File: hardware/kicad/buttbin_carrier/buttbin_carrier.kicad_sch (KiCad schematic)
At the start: 49 parts, among them J1 USB-C 6P, U1 TP4056, U3 TPS7A0333DBVR, U4 TB-03F-AT_Mesh

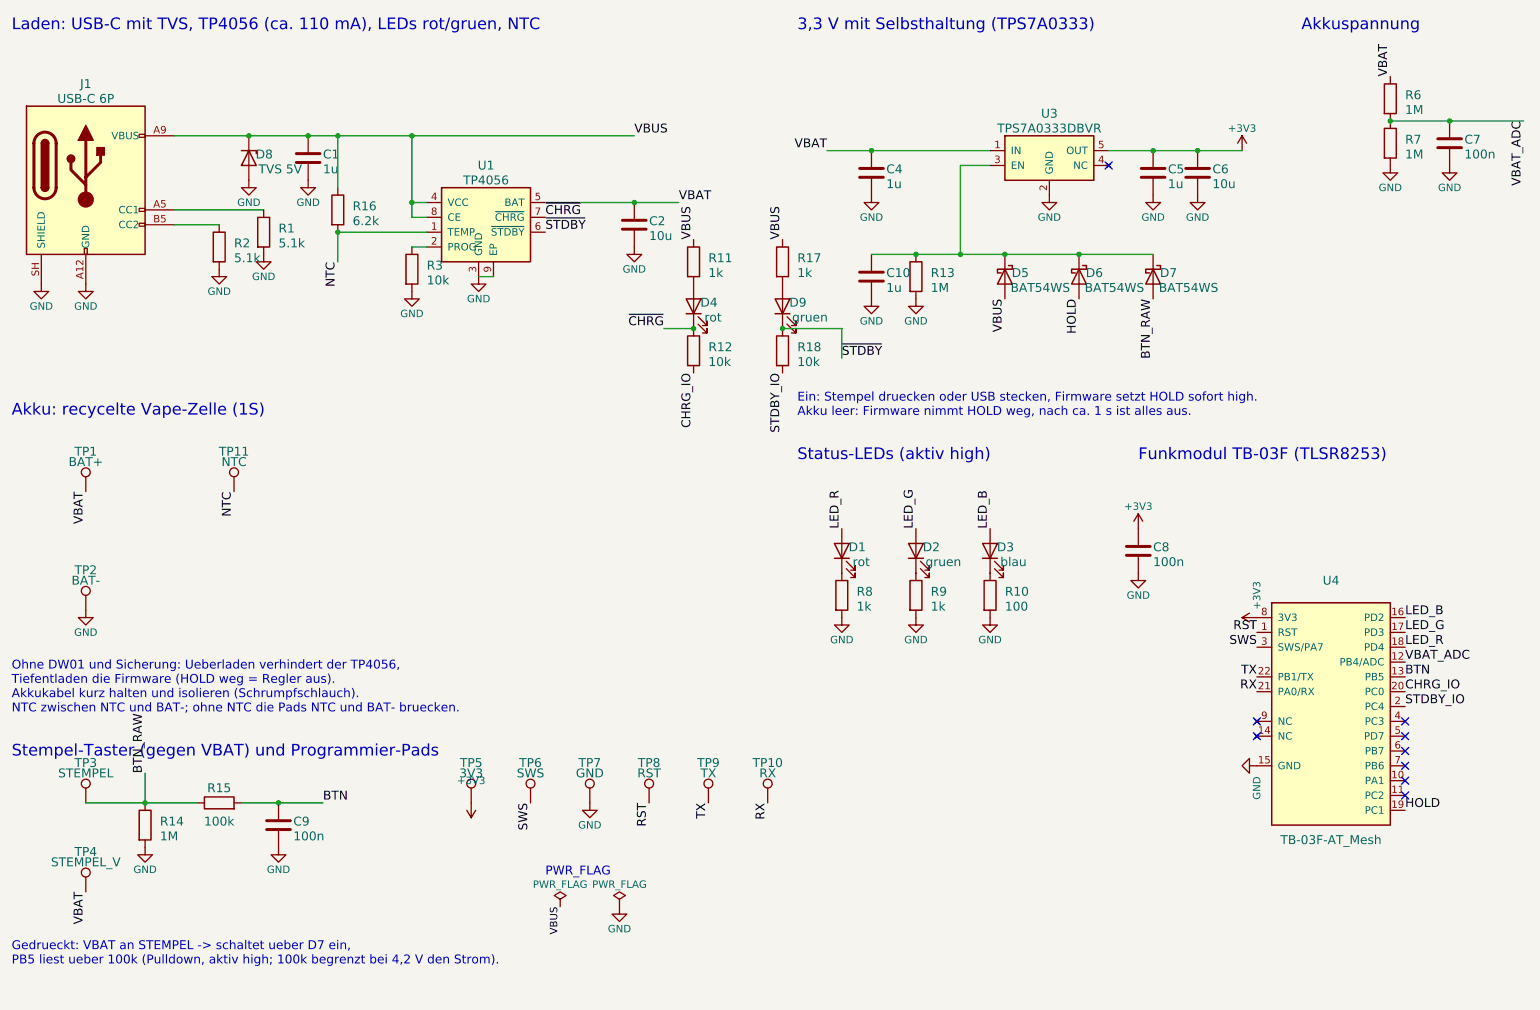
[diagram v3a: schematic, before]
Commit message: Butt Bin board: schematic rev 0.5 with CR2450 coin cell
Switch from a rechargeable recycled cell to a CR2450 coin cell: the
TLSR8253 runs directly from 1.8-3.6 V, so USB-C, TVS, TP4056 with NTC,
LDO with power latch and the battery divider are all gone.

- 100 uF ceramic + 10 uF + 100 nF buffer the TX current peaks
- estimated 12-20 uA average -> about 2-4 years per CR2450
- plunger switch to GND with internal pull-up (as on the dev board)
- red and green LEDs only (blue needs about 3 V)
- holder footprint is a placeholder (Keystone 3008)

Co-Authored-By: Claude Opus 5.5 <noreply@anthropic.com>
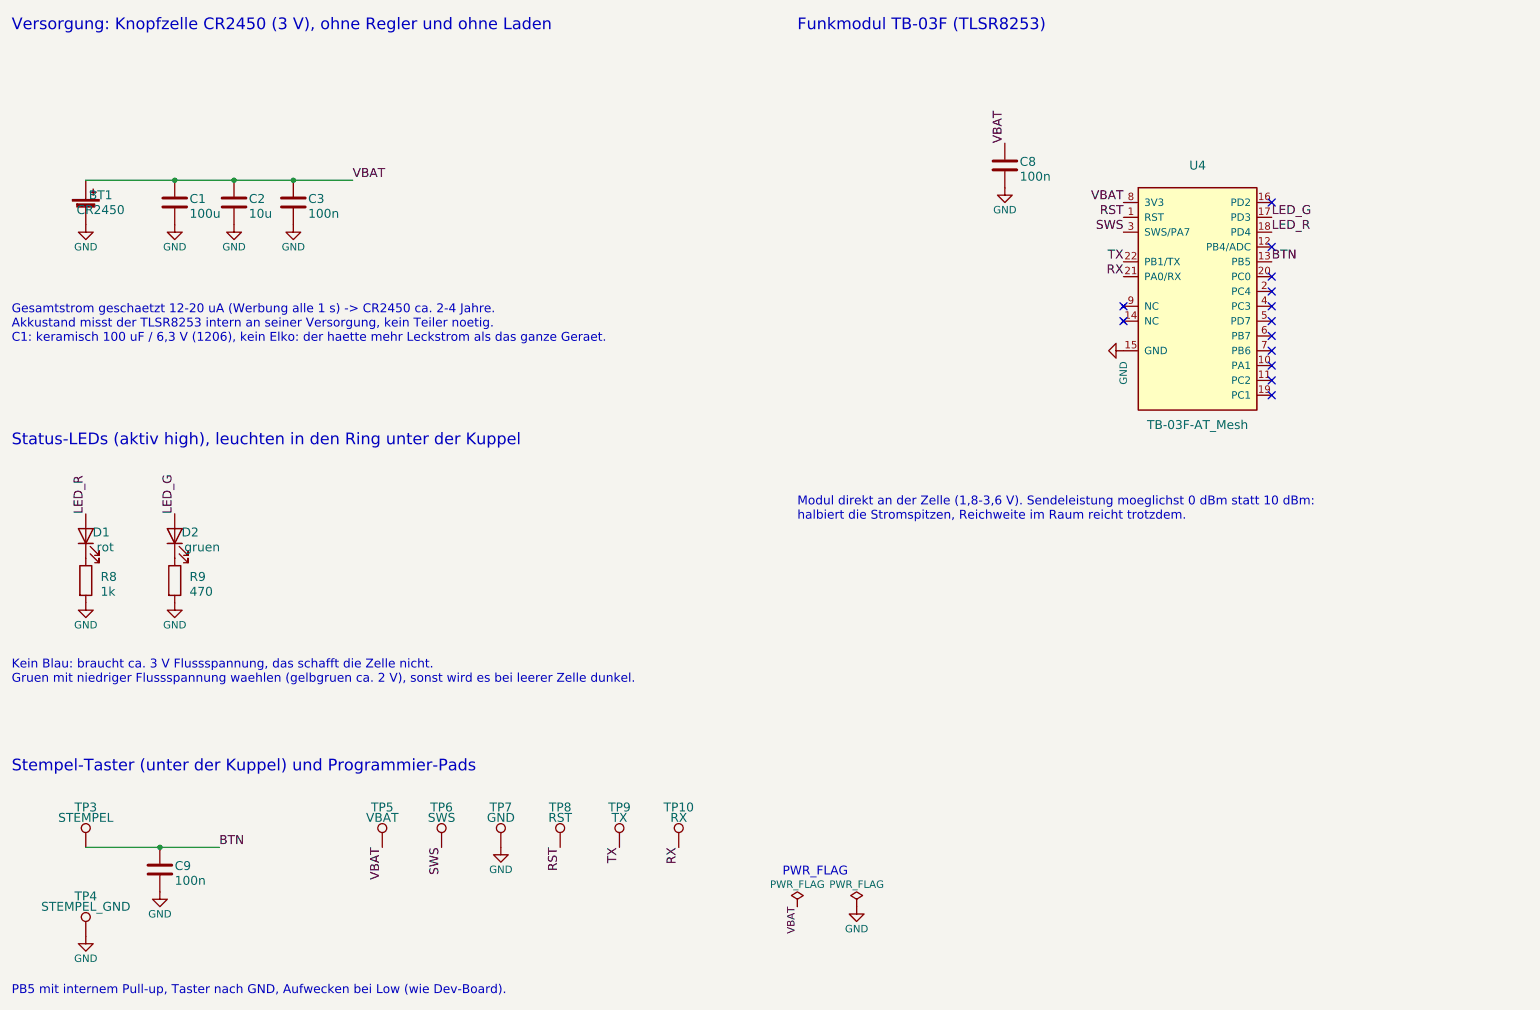
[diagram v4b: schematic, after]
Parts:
- removed C10, C4, C5: 1u, Capacitor_SMD:C_0402_1005Metric, symbol Device:C
- removed C6: 10u, Capacitor_SMD:C_0402_1005Metric, symbol Device:C
- removed C7: 100n, Capacitor_SMD:C_0402_1005Metric, symbol Device:C
- removed D3: blau, LED_SMD:LED_0603_1608Metric, symbol Device:LED
- removed D4: rot, LED_SMD:LED_0603_1608Metric, symbol Device:LED
- removed D5, D6, D7: BAT54WS, Diode_SMD:D_SOD-323, symbol Device:D_Schottky
- removed D8: TVS 5V, Diode_SMD:D_SOD-323, symbol Device:D_Zener
- removed D9: gruen, LED_SMD:LED_0603_1608Metric, symbol Device:LED
- removed J1: USB-C 6P, Connector_USB:USB_C_Receptacle_GCT_USB4125-xx-x_6P_TopMnt_Horizontal, symbol Connector:USB_C_Receptacle_PowerOnly_6P
- removed R1, R2: 5.1k, Resistor_SMD:R_0402_1005Metric, symbol Device:R
- removed R10: 100, Resistor_SMD:R_0402_1005Metric, symbol Device:R
- removed R11, R17: 1k, Resistor_SMD:R_0402_1005Metric, symbol Device:R
- removed R12, R18, R3: 10k, Resistor_SMD:R_0402_1005Metric, symbol Device:R
- removed R13, R14, R6, R7: 1M, Resistor_SMD:R_0402_1005Metric, symbol Device:R
- removed R15: 100k, Resistor_SMD:R_0402_1005Metric, symbol Device:R
- removed R16: 6.2k, Resistor_SMD:R_0402_1005Metric, symbol Device:R
- removed TP1: BAT+, TestPoint:TestPoint_Pad_2.0x2.0mm, symbol Connector:TestPoint
- removed TP11: NTC, TestPoint:TestPoint_Pad_1.0x1.0mm, symbol Connector:TestPoint
- removed TP2: BAT-, TestPoint:TestPoint_Pad_2.0x2.0mm, symbol Connector:TestPoint
- removed U1: TP4056, Package_SO:SOIC-8-1EP_3.9x4.9mm_P1.27mm_EP2.29x3mm, symbol ButtBin:TP4056
- removed U3: TPS7A0333DBVR, Package_TO_SOT_SMD:SOT-23-5, symbol ButtBin:TPS7A0333DBV
- added BT1: CR2450, Battery:BatteryHolder_Keystone_3008_1x2450, symbol Device:Battery_Cell
- added C3: 100n, Capacitor_SMD:C_0402_1005Metric, symbol Device:C
- C1: value 1u -> 100u; LCSC C52923 -> (none)
- R9: value 1k -> 470; LCSC C11702 -> (none)
- TP3: Hinweis Taster zwischen STEMPEL und STEMPEL_V -> Taster zwischen STEMPEL und STEMPEL_GND
- TP4: value STEMPEL_V -> STEMPEL_GND
- TP5: value 3V3 -> VBAT
- U4: Hinweis Antenne ueber Platinenrand, im Griff nur Kunststoff darueber -> Antenne nach oben in die Harzkuppel, kein Metall darueber
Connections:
- net +3V3 is gone; now on net VBAT: C8.1, TP5.1, U4.8 (3V3)
- net BTN_RAW is gone; now on net BTN: TP3.1
- net VBUS is gone; now on net VBAT: C1.1
- net GND: now also TP4.1, BT1.2 (-), C3.2
- net VBAT: now also BT1.1 (+), C3.1; no longer TP4.1
- net CHRG_IO: no longer names the net of U4.20 (PC0)
- net HOLD: no longer names the net of U4.19 (PC1)
- net LED_B: no longer names the net of U4.16 (PD2)
- net STDBY_IO: no longer names the net of U4.2 (PC4)
- net VBAT_ADC: no longer names the net of U4.12 (PB4/ADC)
- no-connect marks 9 -> 13
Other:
- note added: "Gesamtstrom geschaetzt 12-20 uA (Werbung alle 1 s) -> CR2450 ca. 2-4 Jahre. Akkustand misst der TLSR8253 intern an seiner Versorgung, kein Teiler noetig. C1: keramisch 100 uF / 6,3 V (1206), kein Elko: der haette mehr Leckstrom als das ganze Geraet."
- note added: "Kein Blau: braucht ca. 3 V Flussspannung, das schafft die Zelle nicht. Gruen mit niedriger Flussspannung waehlen (gelbgruen ca. 2 V), sonst wird es bei leerer Zelle dunkel."
- note added: "Modul direkt an der Zelle (1,8-3,6 V). Sendeleistung moeglichst 0 dBm statt 10 dBm: halbiert die Stromspitzen, Reichweite im Raum reicht trotzdem."
- note added: "PB5 mit internem Pull-up, Taster nach GND, Aufwecken bei Low (wie Dev-Board)."
- note added: "Status-LEDs (aktiv high), leuchten in den Ring unter der Kuppel"
- note added: "Stempel-Taster (unter der Kuppel) und Programmier-Pads"
- note added: "Versorgung: Knopfzelle CR2450 (3 V), ohne Regler und ohne Laden"
- note removed: "3,3 V mit Selbsthaltung (TPS7A0333)"
- note removed: "Akku: recycelte Vape-Zelle (1S)"
- note removed: "Akkuspannung"
- note removed: "Ein: Stempel druecken oder USB stecken, Firmware setzt HOLD sofort high. Akku leer: Firmware nimmt HOLD weg, nach ca. 1 s ist alles aus."
- note removed: "Gedrueckt: VBAT an STEMPEL -> schaltet ueber D7 ein, PB5 liest ueber 100k (Pulldown, aktiv high; 100k begrenzt bei 4,2 V den Strom)."
- note removed: "Laden: USB-C mit TVS, TP4056 (ca. 110 mA), LEDs rot/gruen, NTC"
- note removed: "Ohne DW01 und Sicherung: Ueberladen verhindert der TP4056, Tiefentladen die Firmware (HOLD weg = Regler aus). Akkukabel kurz halten und isolieren (Schrumpfschlauch). NTC zwischen NTC und BAT-; ohne NTC die Pads NTC und BAT- bruecken."
- note removed: "Status-LEDs (aktiv high)"
- note removed: "Stempel-Taster (gegen VBAT) und Programmier-Pads"

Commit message: Butt Bin board: nine individually driven ring LEDs
Red, yellow and green alternating around the light ring under the resin
dome, each on its own GPIO with 1k (about 1 mA); LED_1..5 on PWM0..4 for
dimming, LED_6..9 on/off. Only low forward voltage colours, so they stay
bright until the CR2450 is empty.

Co-Authored-By: Claude Opus 5.5 <noreply@anthropic.com>
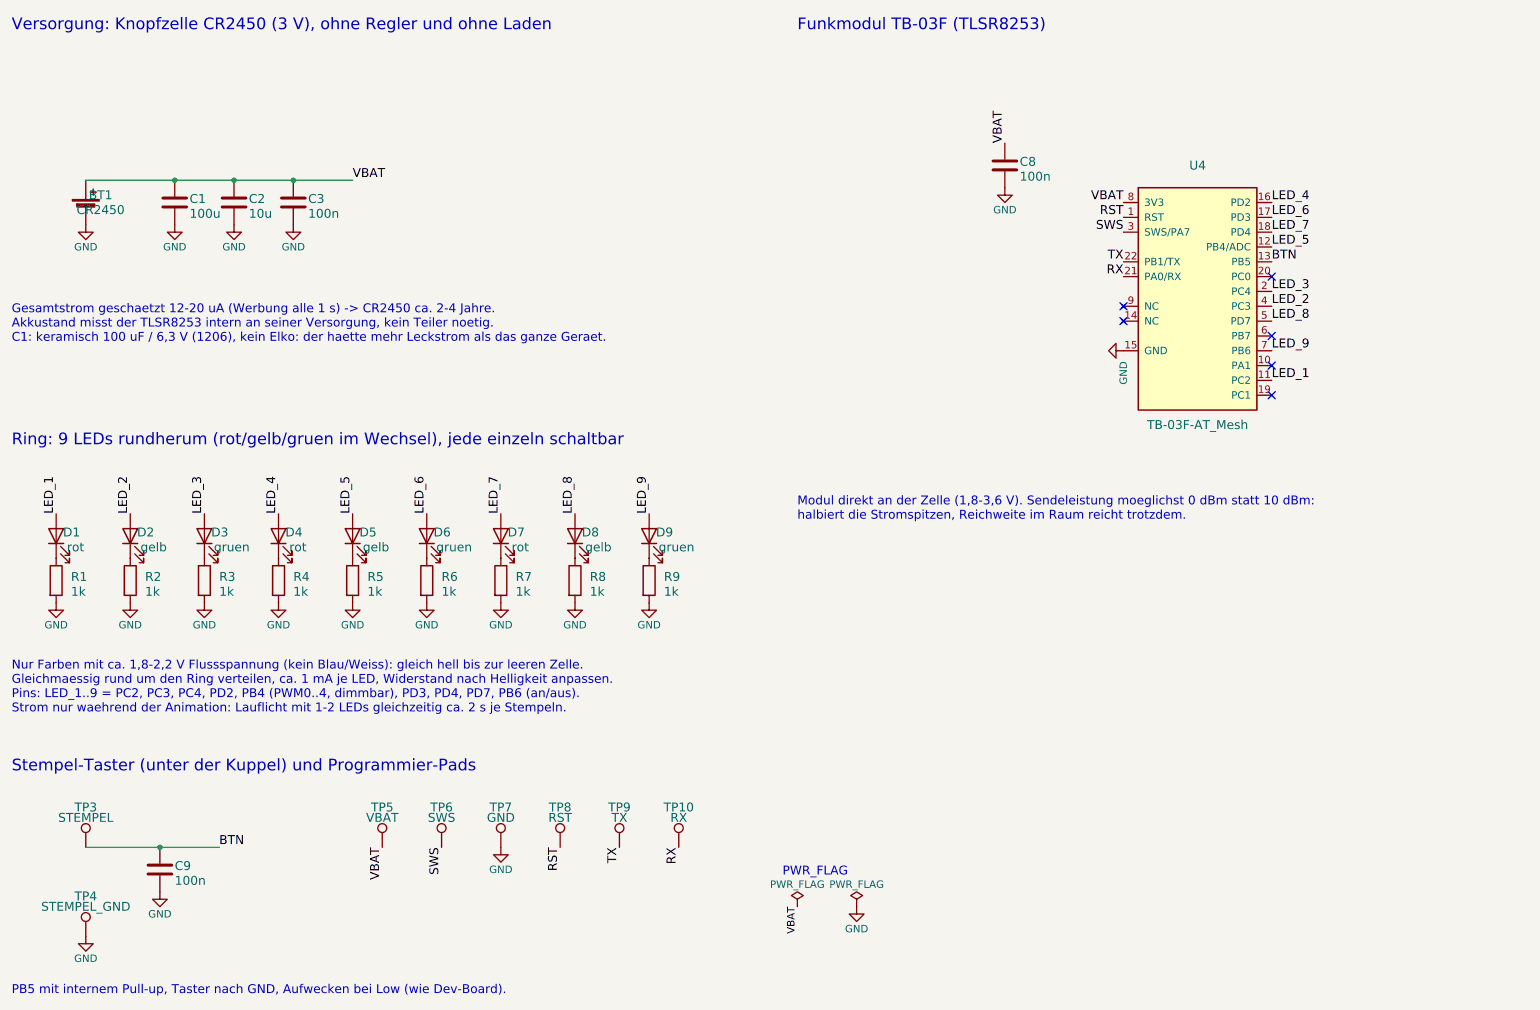
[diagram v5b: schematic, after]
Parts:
- added D3, D6, D9: gruen, LED_SMD:LED_0603_1608Metric, symbol Device:LED
- added D4, D7: rot, LED_SMD:LED_0603_1608Metric, symbol Device:LED
- added D5, D8: gelb, LED_SMD:LED_0603_1608Metric, symbol Device:LED
- added R1, R2, R3, R4, R5, R6, R7: 1k, Resistor_SMD:R_0402_1005Metric, symbol Device:R
- D2: value gruen -> gelb; LCSC C72043 -> (none)
- R9: value 470 -> 1k; LCSC (none) -> C11702
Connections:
- net GND: now also R1.2, R2.2, R3.2, R4.2, R5.2, R6.2, R7.2
- net at D2.1 (K): now also R2.1; no longer R9.1
- net at R8.1: now also D8.1 (K); no longer D1.1 (K)
- net LED_1: now reaches U4.11 (PC2)
- net LED_1: now also D1.2 (A)
- net LED_5: now reaches U4.12 (PB4/ADC)
- net LED_5: now also D5.2 (A)
- net LED_4: now reaches U4.16 (PD2)
- net LED_4: now also D4.2 (A)
- net LED_3: now reaches U4.2 (PC4)
- net LED_3: now also D3.2 (A)
- net LED_2: now reaches U4.4 (PC3)
- net LED_2: now also D2.2 (A)
- net LED_8: now reaches U4.5 (PD7)
- net LED_8: now also D8.2 (A)
- net LED_9: now reaches U4.7 (PB6)
- net LED_9: now also D9.2 (A)
- net LED_G renamed LED_6
- net LED_6: now also D6.2 (A); no longer D2.2 (A)
- net LED_R renamed LED_7
- net LED_7: now also D7.2 (A); no longer D1.2 (A)
- new net: D1.1 (K), R1.1
- new net: D6.1 (K), R6.1
- new net: D5.1 (K), R5.1
- new net: D7.1 (K), R7.1
- new net: D4.1 (K), R4.1
- new net: D3.1 (K), R3.1
- new net: D9.1 (K), R9.1
- no-connect marks 13 -> 6
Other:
- note added: "Nur Farben mit ca. 1,8-2,2 V Flussspannung (kein Blau/Weiss): gleich hell bis zur leeren Zelle. Gleichmaessig rund um den Ring verteilen, ca. 1 mA je LED, Widerstand nach Helligkeit anpassen. Pins: LED_1..9 = PC2, PC3, PC4, PD2, PB4 (PWM0..4, dimmbar), PD3, PD4, PD7, PB6 (an/aus). Strom nur waehrend der Animation: Lauflicht mit 1-2 LEDs gleichzeitig ca. 2 s je Stempeln."
- note added: "Ring: 9 LEDs rundherum (rot/gelb/gruen im Wechsel), jede einzeln schaltbar"
- note removed: "Kein Blau: braucht ca. 3 V Flussspannung, das schafft die Zelle nicht. Gruen mit niedriger Flussspannung waehlen (gelbgruen ca. 2 V), sonst wird es bei leerer Zelle dunkel."
- note removed: "Status-LEDs (aktiv high), leuchten in den Ring unter der Kuppel"

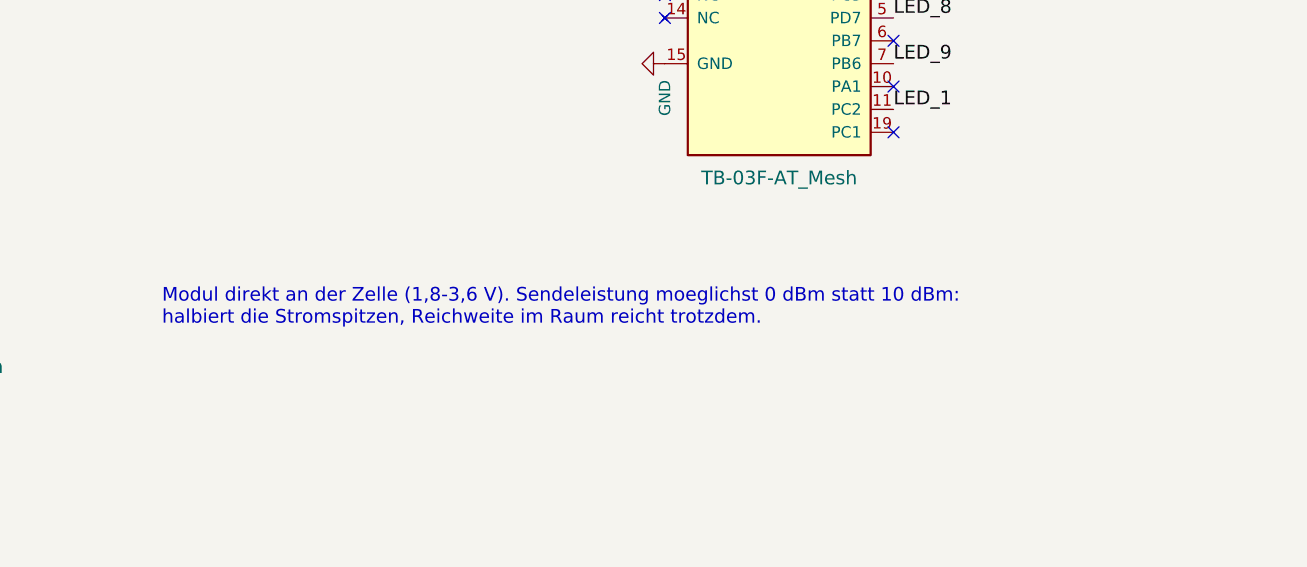
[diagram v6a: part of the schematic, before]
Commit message: Butt Bin board: add the PB7 battery note (missing in previous commit)
Co-Authored-By: Claude Opus 5.5 <noreply@anthropic.com>
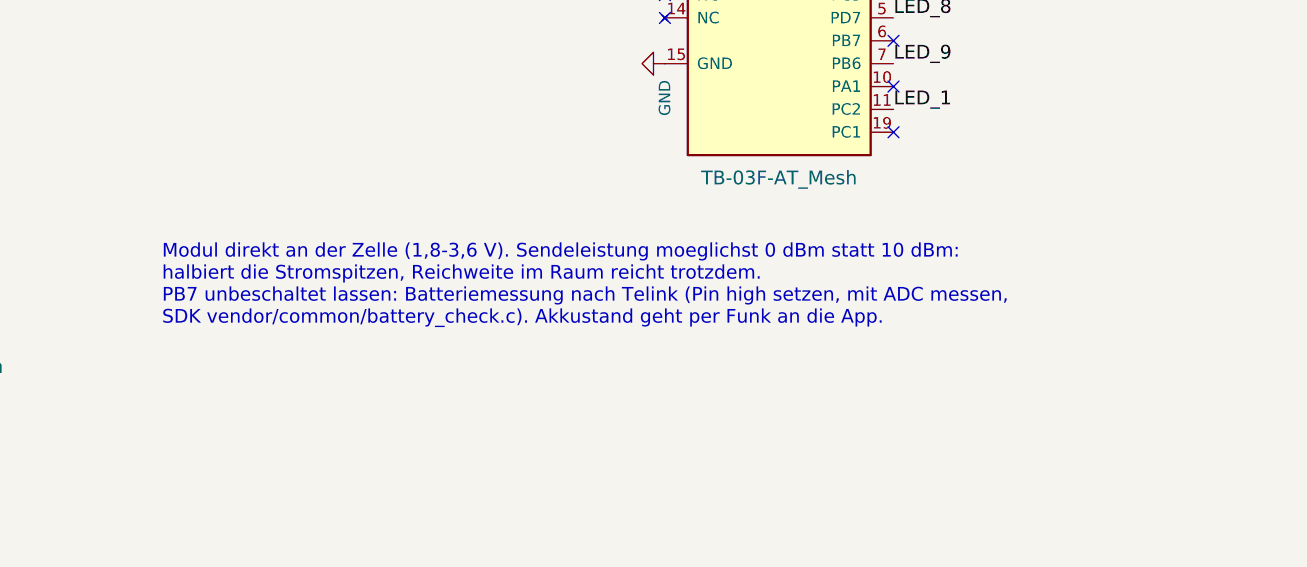
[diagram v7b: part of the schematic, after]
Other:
- note added: "Modul direkt an der Zelle (1,8-3,6 V). Sendeleistung moeglichst 0 dBm statt 10 dBm: halbiert die Stromspitzen, Reichweite im Raum reicht trotzdem. PB7 unbeschaltet lassen: Batteriemessung nach Telink (Pin high setzen, mit ADC messen, SDK vendor/common/battery_check.c). Akkustand geht per Funk an die App."
- note removed: "Modul direkt an der Zelle (1,8-3,6 V). Sendeleistung moeglichst 0 dBm statt 10 dBm: halbiert die Stromspitzen, Reichweite im Raum reicht trotzdem."
